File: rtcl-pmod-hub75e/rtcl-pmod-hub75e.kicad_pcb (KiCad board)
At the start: 2 copper layers, 20 x 13 mm, 19 parts, among them J1 PMOD, J2 HIF3FC-16PA-2.54DSA(71), U1 74LVC273, U2 74LVC273, U3 74LVC273, U4 74LVC273, U5 LM809M3-2.93, U6 74LVC2G86

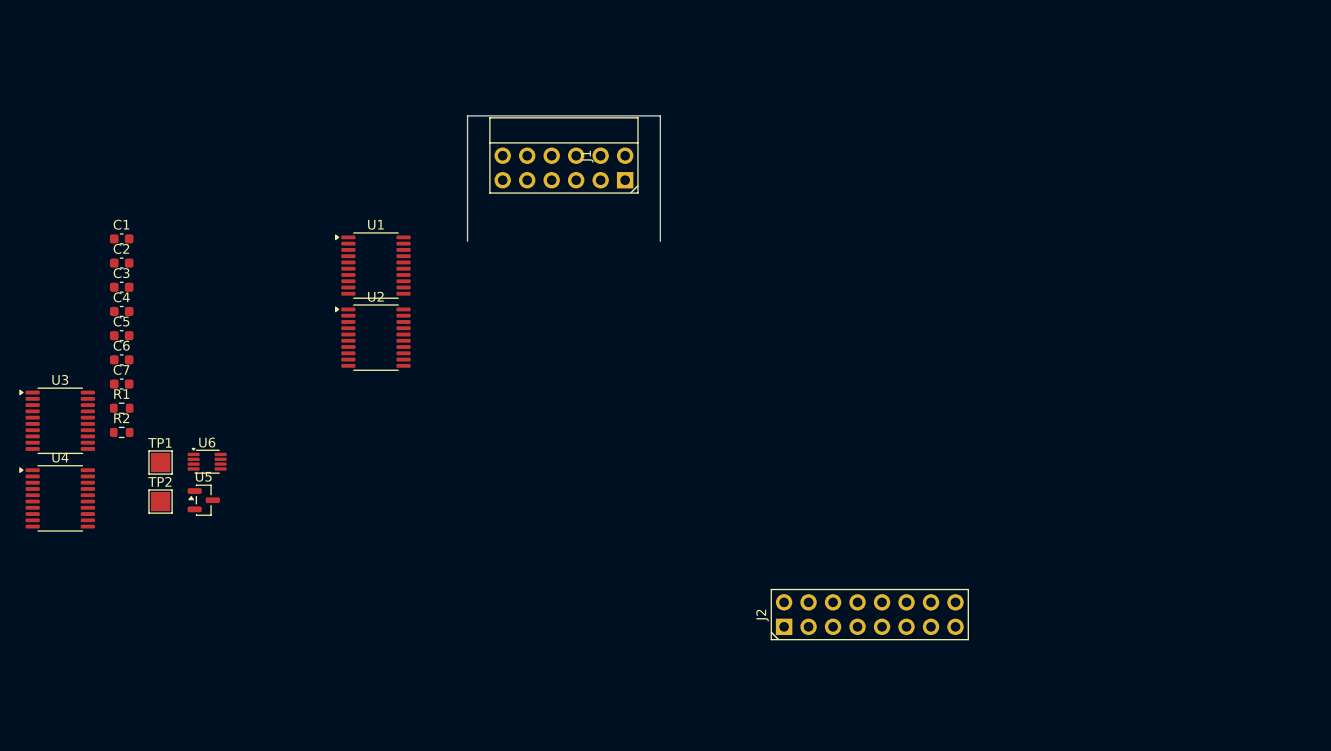
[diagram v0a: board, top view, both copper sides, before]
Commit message: Refactor PH_02x06_2.54mm.kicad_mod: Update properties, adjust pin positions, and modify silk screen lines for improved clarity and accuracy
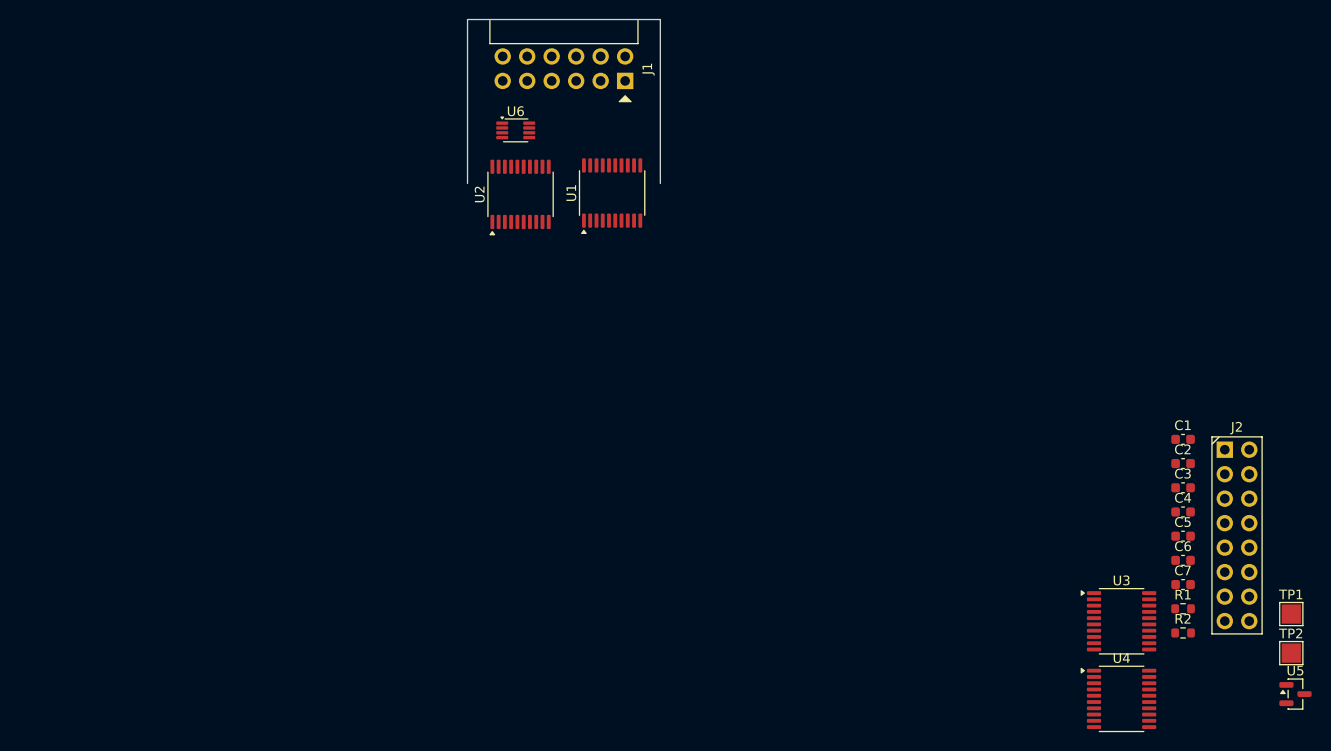
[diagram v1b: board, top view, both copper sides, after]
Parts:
- moved TP1 118.3 mm to (185.5, 111.7)
- moved TP2 118.3 mm to (185.5, 115.7)
- moved U5 115.0 mm to (185.9, 120.0)
- moved C1 112.0 mm to (174.2, 93.6)
- moved C2 112.0 mm to (174.2, 96.1)
- moved C3 112.0 mm to (174.2, 98.6)
- moved C4 112.0 mm to (174.2, 101.1)
- moved C5 112.0 mm to (174.2, 103.6)
- moved C6 112.0 mm to (174.2, 106.1)
- moved C7 112.0 mm to (174.2, 108.6)
- moved R1 112.0 mm to (174.2, 111.1)
- moved R2 112.0 mm to (174.2, 113.6)
- moved U3 112.0 mm to (167.8, 112.4)
- moved U4 112.0 mm to (167.8, 120.5)
- moved J2 49.3 mm to (178.6, 94.6), turned to 0 degrees
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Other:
- board size 20 x 13 mm -> 20 x 17 mm

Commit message: Update design rules and footprint for PH_02x08_2.54mm header
- Modified differential pair dimensions and DRC exclusions in the project configuration.
- Adjusted various design rule checks (DRC) to change warnings to errors or ignore them as necessary.
- Updated minimum clearance and hole clearance values for better manufacturability.
- Changed track widths and via dimensions to accommodate new design requirements.
- Revised the footprint for PH_02x08_2.54mm header, including repositioning properties and updating UUIDs for pads and lines.
- Ensured all pads are correctly placed and sized for optimal performance.
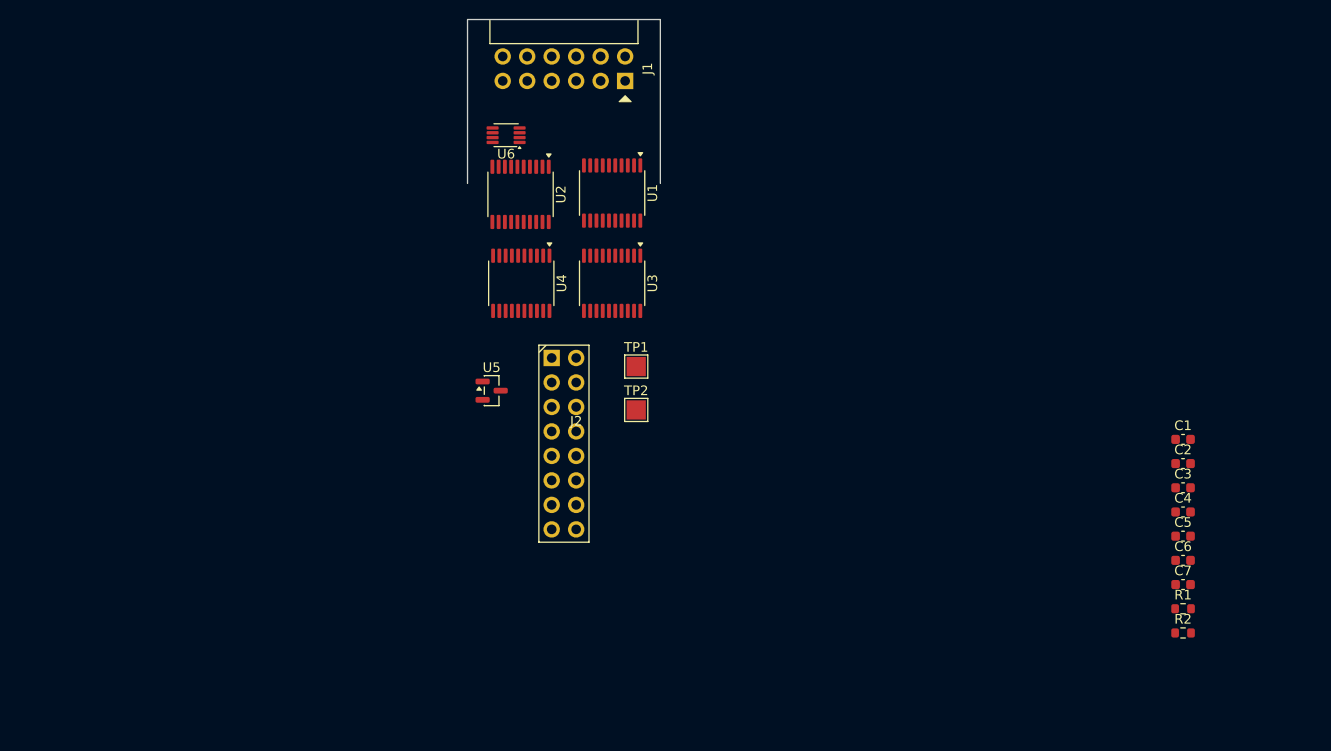
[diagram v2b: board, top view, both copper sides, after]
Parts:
- moved U5 89.1 mm to (102.5, 88.5)
- moved U4 75.7 mm to (105.6, 77.4), turned to -90 degrees
- moved TP1 72.6 mm to (117.5, 86.0)
- moved TP2 72.5 mm to (117.5, 90.5)
- moved J2 68.6 mm to (110.0, 94.0)
- moved U3 63.4 mm to (115.0, 77.4), turned to -90 degrees
- moved U6 1.12 mm to (104.0, 62.0), turned to 180 degrees
- turned U1 to -90 degrees
- turned U2 to -90 degrees

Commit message: Refactor code structure for improved readability and maintainability
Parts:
- added J3: Conn_01x02, Connector_PinHeader_2.54mm:PinHeader_1x02_P2.54mm_Vertical, F.Cu at (117.5, 99.0)
- added TP3: TestPoint, TestPoint:TestPoint_Pad_D1.0mm, F.Cu at (118.4, 61.2)
- added TP4: TestPoint, TestPoint:TestPoint_Pad_D1.0mm, F.Cu at (109.5, 61.5)
- TP1, TP2: value Conn_01x01 -> TestPoint; footprint TestPoint:TestPoint_Pad_2.0x2.0mm -> TestPoint:TestPoint_Pad_D1.0mm
- moved C7 85.8 mm to (104.2, 59.0)
- moved R2 84.9 mm to (107.2, 61.5), turned to -90 degrees
- moved C6 81.9 mm to (104.2, 63.6)
- moved R1 76.4 mm to (116.2, 61.4), turned to -90 degrees
- moved C5 72.0 mm to (103.0, 93.0), turned to 180 degrees
- moved C4 69.0 mm to (109.0, 78.5), turned to 90 degrees
- moved C2 69.0 mm to (109.2, 73.0), turned to 90 degrees
- moved C1 60.2 mm to (119.0, 69.5), turned to 90 degrees
- moved C3 58.8 mm to (119.0, 78.5), turned to 90 degrees
- moved TP2 6.32 mm to (115.5, 84.5)
- moved TP1 1.58 mm to (118.0, 84.5)
- moved U4 1.25 mm to (104.5, 78.0)
- moved U5 1.12 mm to (103.5, 89.0)
- moved U2 1.06 mm to (104.5, 68.5)
- moved U3 0.81 mm to (114.5, 78.0)
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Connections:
- net Net-(U1-Q0) renamed /D0P
- net Net-(U1-Q1) renamed /D1P
- net Net-(U1-Q2) renamed /D2P
- net Net-(U1-Q3) renamed /D3P
- net Net-(U1-Q4) renamed /D4P
- net Net-(U1-Q5) renamed /D5P
- net Net-(U1-Q6) renamed /D6P
- net Net-(U1-Q7) renamed /D7P
- net Net-(U2-Q0) renamed /D0N
- net Net-(U2-Q1) renamed /D1N
- net Net-(U2-Q2) renamed /D2N
- net Net-(U2-Q3) renamed /D3N
- net Net-(U2-Q4) renamed /D4N
- net Net-(U2-Q5) renamed /D5N
- net Net-(U2-Q6) renamed /D6N
- net Net-(U2-Q7) renamed /D7N
- U1 pad 13: /PMOD4 -> /PMOD6
- U1 pad 17: /PMOD6 -> /PMOD4
- U2 pad 3: /PMOD0 -> /PMOD3
- U2 pad 4: /PMOD1 -> /PMOD2
- U2 pad 7: /PMOD2 -> /PMOD1
- U2 pad 8: /PMOD3 -> /PMOD0
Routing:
- net /PMOD5: track 0.00 -> 31.9 mm, vias 0 -> 1
- net /PMOD0: track 0.00 -> 27.3 mm
- net /PMOD6: track 0.00 -> 26.1 mm, vias 0 -> 1
- net /PMOD1: track 0.00 -> 24.3 mm
- net /PMOD4: track 0.00 -> 22.6 mm, vias 0 -> 1
- net /PMOD2: track 0.00 -> 20.2 mm
- net /PMOD3: track 0.00 -> 19.4 mm
- net /D1P: track 0.00 -> 13.7 mm, vias 0 -> 2
- net /PMOD7: track 0.00 -> 13.4 mm
- net Net-(U1-D7): track 0.00 -> 11.1 mm
- net /D2P: track 0.00 -> 9.79 mm, vias 0 -> 2
- net /D0P: track 0.00 -> 9.77 mm, vias 0 -> 2
- net Net-(U2-D7): track 0.00 -> 7.77 mm, vias 0 -> 1
- net /D7P: track 0.00 -> 1.29 mm
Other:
- board size 20 x 17 mm -> 20 x 56 mm
- copper layers 2 -> 4

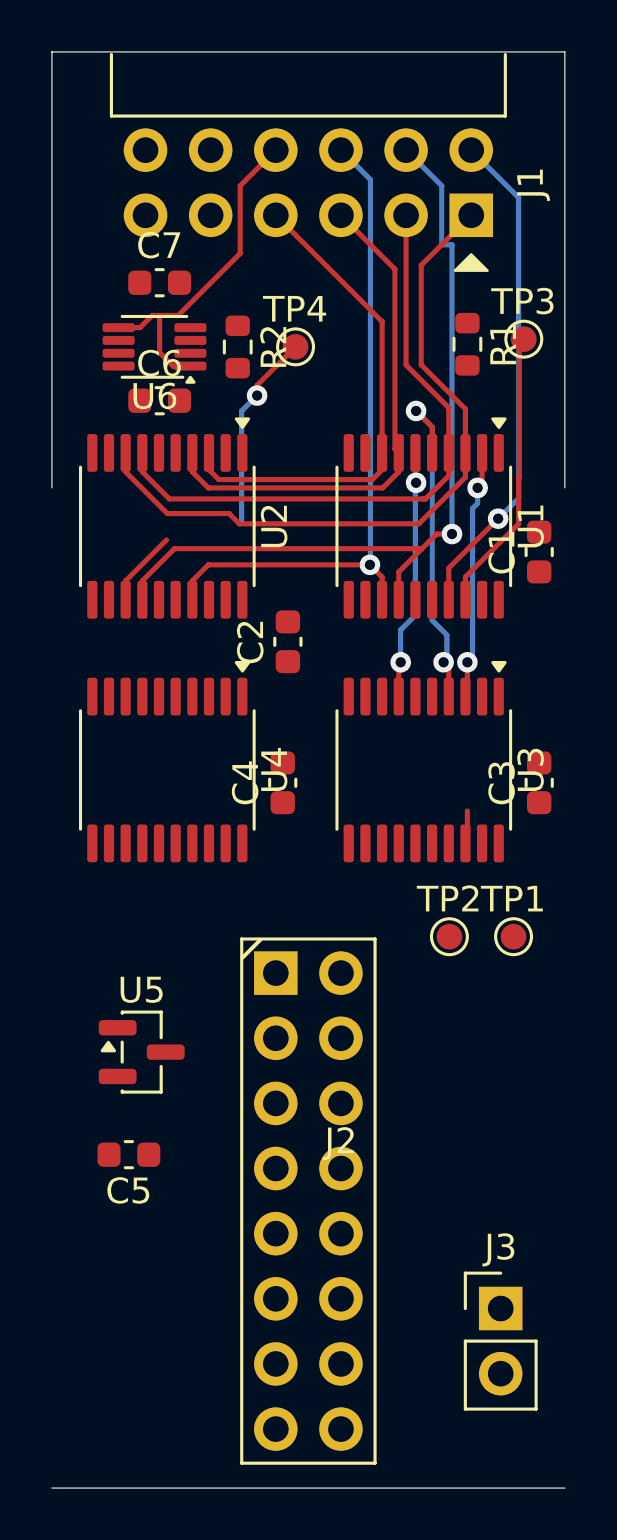
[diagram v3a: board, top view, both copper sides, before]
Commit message: Update PCB design parameters and wire connections in the rtcl-pmod-hub75e project
- Changed active layer from 0 to 2 in the project settings.
- Cleared used designators in the project file for better clarity.
- Adjusted multiple wire connection points in the schematic to correct coordinates for improved layout.
- Updated label positions for various components to reflect new wire connections and ensure proper alignment.
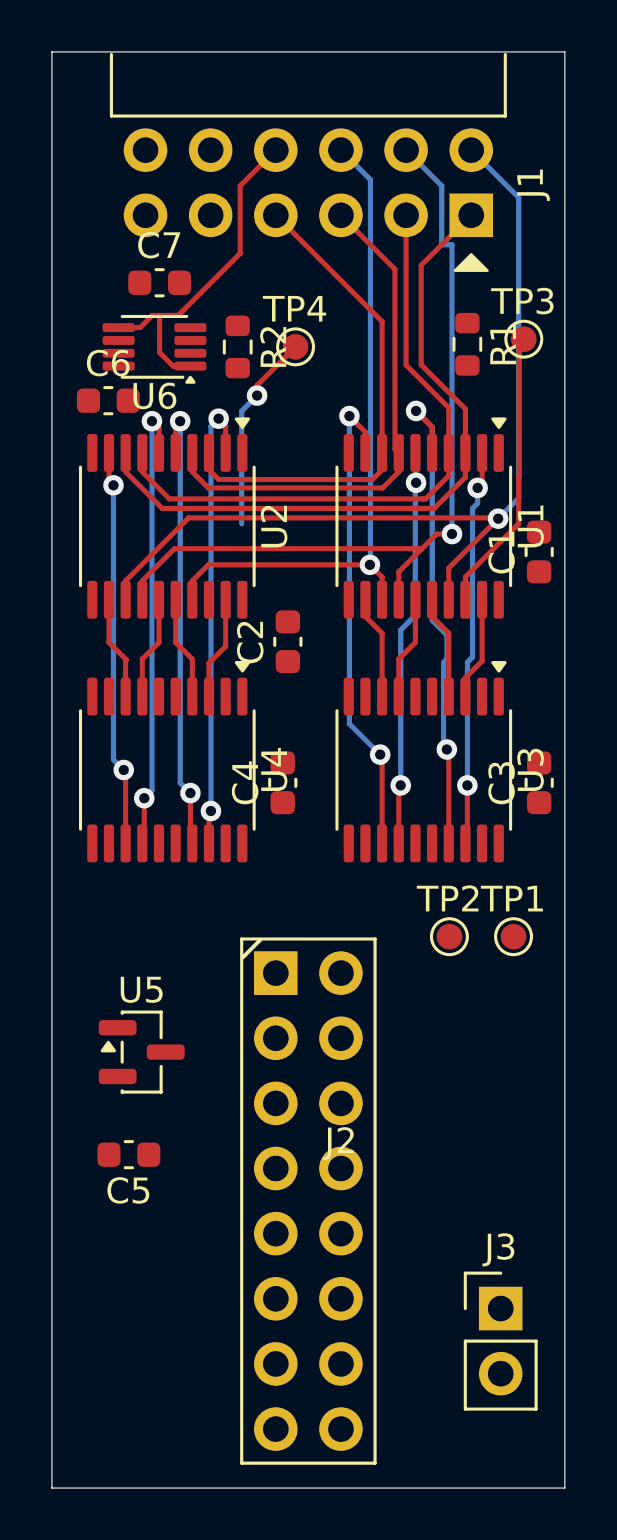
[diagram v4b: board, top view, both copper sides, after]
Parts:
- moved C6 2.00 mm to (102.2, 63.6)
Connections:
- U1 pad 12: /D4P -> /D6P
- U1 pad 16: /D6P -> /D4P
- U3 pad 13: /D4P -> /D3P
- U3 pad 14: /D5P -> /D2P
- U3 pad 17: /D6P -> /D1P
- U3 pad 18: /D7P -> /D0P
- U3 pad 3: /D0P -> /D7P
- U3 pad 4: /D1P -> /D4P
- U3 pad 7: /D2P -> /D5P
- U3 pad 8: /D3P -> /D6P
- U4 pad 13: /D4N -> /D3N
- U4 pad 14: /D5N -> /D2N
- U4 pad 17: /D6N -> /D1N
- U4 pad 18: /D7N -> /D0N
- U4 pad 3: /D0N -> /D7N
- U4 pad 4: /D1N -> /D6N
- U4 pad 7: /D2N -> /D5N
- U4 pad 8: /D3N -> /D4N
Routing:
- net /D3P: track 0.00 -> 18.9 mm, vias 0 -> 2
- net /D0N: track 0.00 -> 18.2 mm, vias 0 -> 2
- net /D2N: track 0.00 -> 18.0 mm, vias 0 -> 2
- net /D1N: track 0.00 -> 18.0 mm, vias 0 -> 2
- net /D3N: track 0.00 -> 15.5 mm, vias 0 -> 2
- net /PMOD4: track 22.6 -> 35.9 mm
- net /D2P: track 9.79 -> 15.5 mm
- net /D1P: track 13.7 -> 19.4 mm
- net /D0P: track 9.77 -> 15.5 mm
- net /D4P: track 0.00 -> 4.08 mm
- net /D4N: track 0.00 -> 4.06 mm
- net /D7N: track 0.00 -> 4.04 mm
- net /D6N: track 0.00 -> 4.04 mm
- net /D5P: track 0.00 -> 4.04 mm
- net /D5N: track 0.00 -> 4.04 mm
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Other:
- outline, holes or cut-outs redrawn

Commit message: Update PCB layout settings: change active layer to 0 and adjust selection filter options
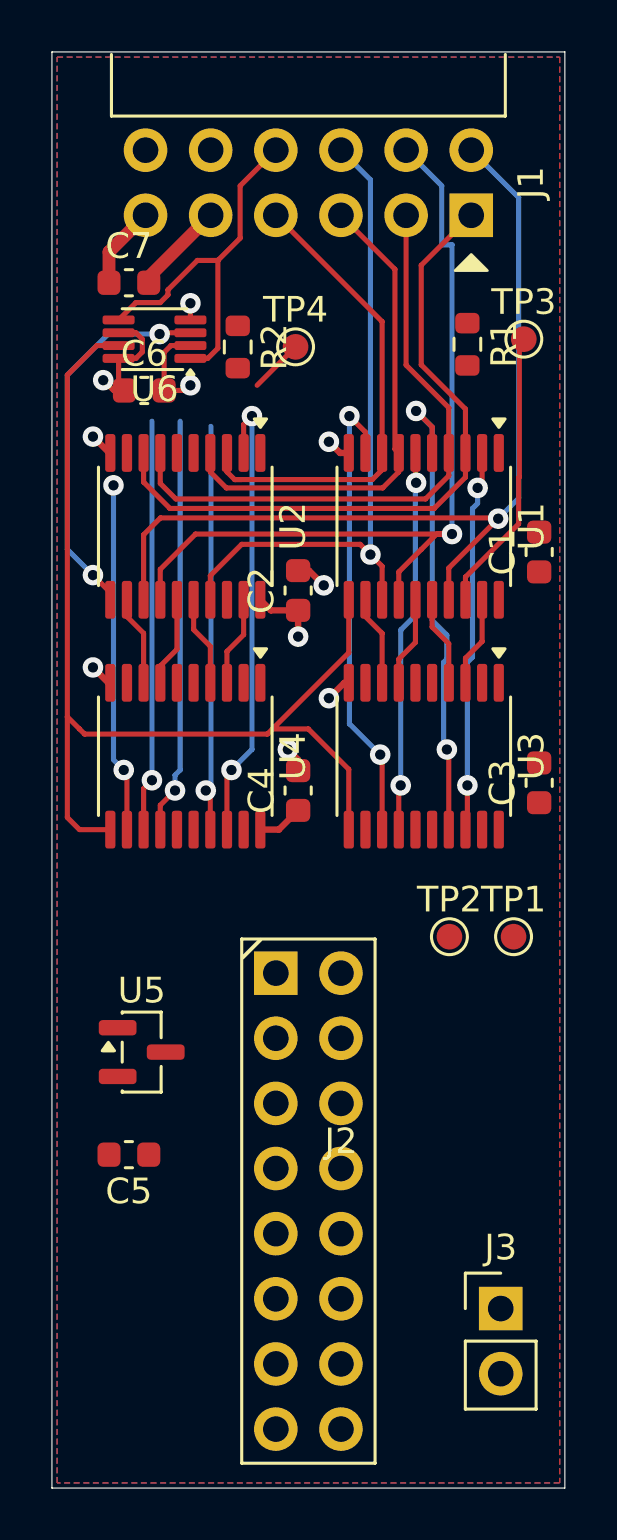
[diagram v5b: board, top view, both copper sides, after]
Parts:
- moved C2 2.04 mm to (109.6, 71.0)
- moved C6 1.46 mm to (103.6, 63.2)
- moved C7 1.20 mm to (103.0, 59.0)
- moved U4 0.88 mm to (105.2, 77.5)
- moved U2 0.70 mm to (105.2, 68.5)
- moved C4 0.67 mm to (109.6, 78.8)
- moved U3 0.54 mm to (114.5, 77.5)
- moved U6 0.30 mm to (104.0, 61.2)
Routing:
- net /CLK_P: track 0.00 -> 42.7 mm
- net /CLK_N: track 0.00 -> 14.7 mm, vias 0 -> 2
- net GND: track 0.00 -> 14.1 mm, vias 0 -> 8
- net /HUB75_R2: track 0.00 -> 13.9 mm, vias 0 -> 2
- net +3.3V: track 0.00 -> 12.6 mm, vias 0 -> 2
- net Net-(U2-D7): track 7.77 -> 2.12 mm, vias 1 -> 0
- net /D1N: track 18.0 -> 15.9 mm, vias 2 -> 1
- net /D2N: track 18.0 -> 16.2 mm, vias 2 -> 1
- net /PMOD7: track 13.4 -> 15.0 mm
- net /PMOD5: track 31.9 -> 32.9 mm
- net /PMOD2: track 20.2 -> 19.5 mm
- net /D7P: track 4.15 -> 3.51 mm
- net /D3N: track 15.5 -> 16.1 mm, vias 2 -> 1
- net /D4N: track 4.06 -> 3.51 mm
- net /D7N: track 4.04 -> 3.51 mm
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- added copper zone on In2.Cu, net +3.3V
- added copper zone on B.Cu, net GND
- added copper zone on F.Cu, net GND
- added copper zone on In1.Cu, net GND
